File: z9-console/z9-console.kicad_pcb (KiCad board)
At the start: 2 copper layers, 89.5 x 55.5 mm, 130 parts, among them J10 Conn_01x04_Pin, J2 LCD 3.2" 240x320 Conn_01x14_P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, J3 JST GH, J5 ST_STDC14 - SAMTEC_FTSH-107-0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, J6 Screw_Terminal_01x06, J7 TC2070 - TAG Connect, J801 USB_C_Receptacle_USB2.0_16P, Q1 AO3400A, Q2 AO3400A, Q701 AO3400A, SW2 SW_Push, SW3 SW_Push, U1 B0505XT-1WR3, U2 ISO1042-Q1, U22 TLV76733DRVx, U3 STM32F427V_G-I_Tx, U4 ST_SENSOR_2, U5 IIS3DHHCTR, U6 LMR14006YDDCR, U7 SN74LVC1G14DRLR, X2 8MHz 20pF

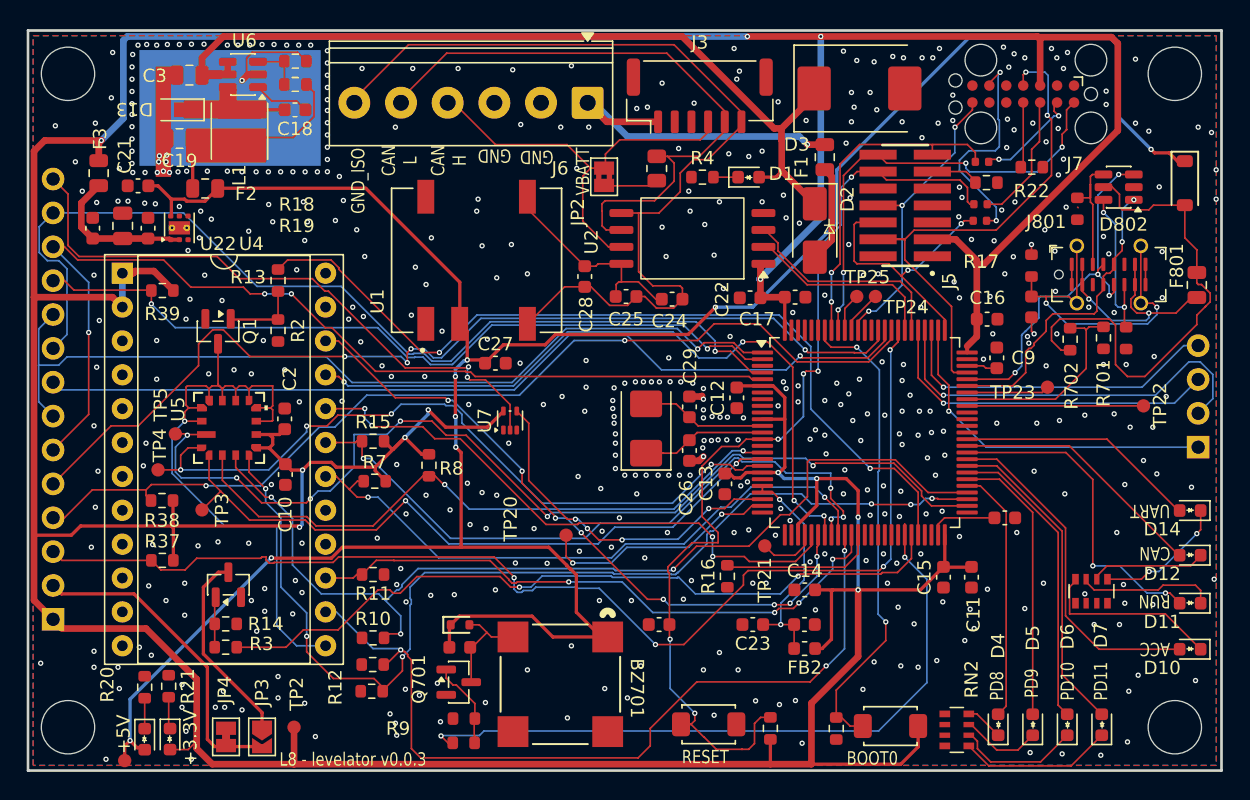
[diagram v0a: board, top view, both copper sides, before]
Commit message: change MEMS device
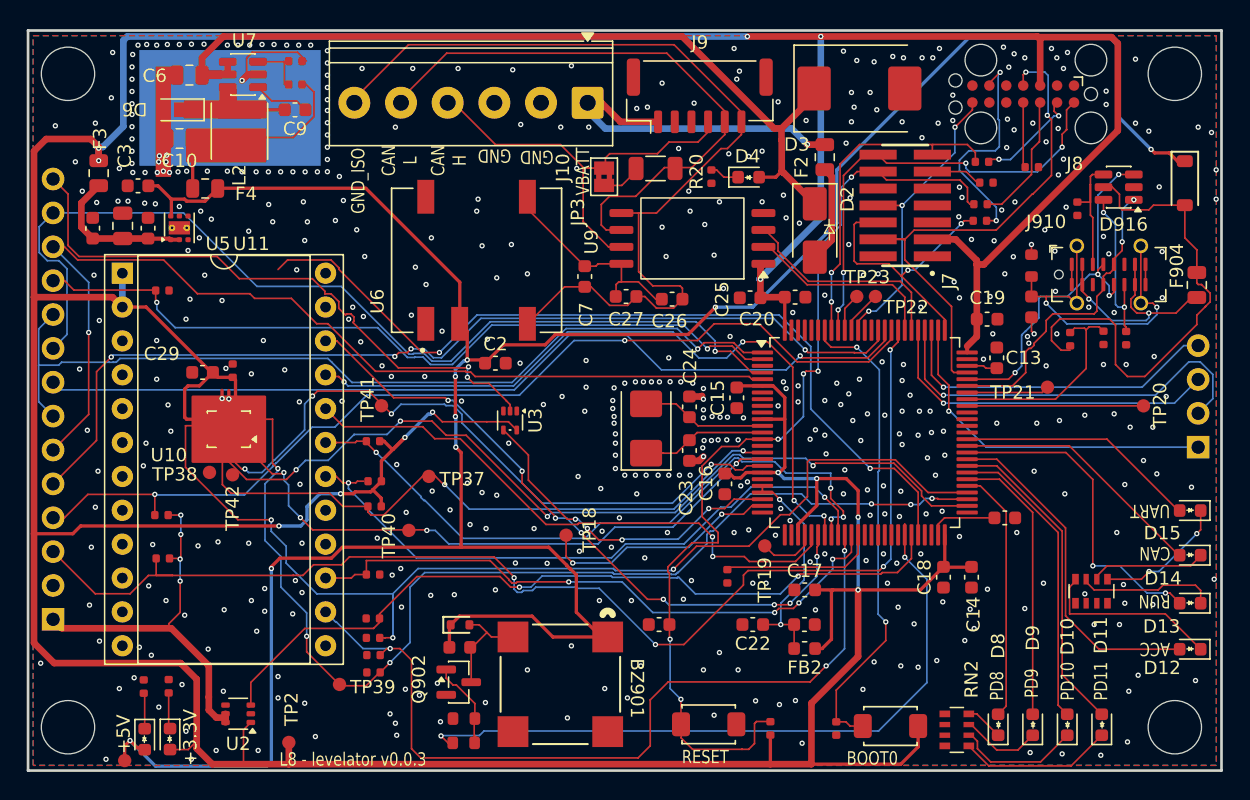
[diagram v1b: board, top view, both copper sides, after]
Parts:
- removed the JP3 at (104.3, 124.8)
- removed JP4: SolderJumper_2_Bridged, Jumper:SolderJumper-2_P1.3mm_Bridged_Pad1.0x1.5mm
- removed Q1, Q2: AO3400A, Package_TO_SOT_SMD:SOT-23
- removed the R13 at (105.5, 90.6)
- removed the R2 at (105.5, 94.3)
- removed the R3 at (101.6, 118.1)
- removed the U5 at (101.8, 101.6)
- added TP37: IIS3DHHCTR_SDI, dnt:TestPoint_Pad_D1.0mm FP .6R, F.Cu at (116.8, 105.2)
- added TP38: IIS3DHHCTR_SDI, dnt:TestPoint_Pad_D1.0mm FP .6R, F.Cu at (100.3, 105.0)
- added TP39: IIS3DHHCTR_SDI, dnt:TestPoint_Pad_D1.0mm FP .6R, F.Cu at (110.1, 120.8)
- added U10: ISM330DHCX, Package_LGA:LGA-14_3x2.5mm_P0.5mm_LayoutBorder3x4y, F.Cu at (101.8, 101.7)
- added U2: TPS22917DBV, dnt:SOT-363_SC-70-6, F.Cu at (102.5, 123.0)
- C28: renamed from C2; footprint Capacitor_SMD:C_0603_1608Metric -> PCM_JLCPCB:C_0402
- R10: renamed from R18; footprint Resistor_SMD:R_0603_1608Metric -> PCM_JLCPCB:R_0402
- R11: renamed from R20; footprint Resistor_SMD:R_0603_1608Metric -> PCM_JLCPCB:R_0402
- R12: renamed from R5; footprint Resistor_SMD:R_0603_1608Metric -> PCM_JLCPCB:R_0402
- R13: renamed from R6; footprint Resistor_SMD:R_0603_1608Metric -> PCM_JLCPCB:R_0402
- R14: renamed from R16; footprint Resistor_SMD:R_0603_1608Metric -> PCM_JLCPCB:R_0402
- R15: renamed from R17; footprint Resistor_SMD:R_0603_1608Metric -> PCM_JLCPCB:R_0402
- R16: renamed from R22; footprint Resistor_SMD:R_0603_1608Metric -> PCM_JLCPCB:R_0402
- R2: renamed from R14; footprint Resistor_SMD:R_0603_1608Metric -> PCM_JLCPCB:R_0402
- R20: renamed from R1; footprint Resistor_SMD:R_0805_2012Metric -> dnt:R_1206_3216Metric
- R21: renamed from R8; footprint Resistor_SMD:R_0603_1608Metric -> PCM_JLCPCB:R_0402
- R22: renamed from R9; footprint Resistor_SMD:R_0603_1608Metric -> PCM_JLCPCB:R_0402
- R23: renamed from R10; footprint Resistor_SMD:R_0603_1608Metric -> PCM_JLCPCB:R_0402
- R24: renamed from R11; footprint Resistor_SMD:R_0603_1608Metric -> PCM_JLCPCB:R_0402
- R25: renamed from R12; footprint Resistor_SMD:R_0603_1608Metric -> PCM_JLCPCB:R_0402
- R26: renamed from R15; footprint Resistor_SMD:R_0603_1608Metric -> PCM_JLCPCB:R_0402
- R27: renamed from R7; footprint Resistor_SMD:R_0603_1608Metric -> PCM_JLCPCB:R_0402
- R3: renamed from R37; footprint Resistor_SMD:R_0603_1608Metric -> PCM_JLCPCB:R_0402
- R4: renamed from R38; footprint Resistor_SMD:R_0603_1608Metric -> PCM_JLCPCB:R_0402
- R5: renamed from R39; footprint Resistor_SMD:R_0603_1608Metric -> PCM_JLCPCB:R_0402
- R7: renamed from R4; footprint Resistor_SMD:R_0603_1608Metric -> PCM_JLCPCB:R_0402
- R8: renamed from R21; footprint Resistor_SMD:R_0603_1608Metric -> PCM_JLCPCB:R_0402
- R9: renamed from R19; footprint Resistor_SMD:R_0603_1608Metric -> PCM_JLCPCB:R_0402
- R930: renamed from R802; footprint PCM_JLCPCB:R_0603 -> PCM_JLCPCB:R_0402
- R931: renamed from R803; value 5.1K -> 5.1kΩ; footprint PCM_JLCPCB:R_0603 -> PCM_JLCPCB:R_0402
- R932: renamed from R702; footprint Resistor_SMD:R_0603_1608Metric -> PCM_JLCPCB:R_0402
- R933: renamed from R701; value 2.2K -> 2.2kΩ; footprint Resistor_SMD:R_0603_1608Metric -> PCM_JLCPCB:R_0402
- moved TP41 17.4 mm to (113.2, 100.0)
- moved TP40 15.6 mm to (115.3, 109.3)
- moved R2 11.0 mm to (112.6, 115.9), turned to 0 degrees
- moved C29 9.86 mm to (99.8, 97.5), turned to 180 degrees
- moved C28 5.32 mm to (102.1, 97.3)
- moved TP42 5.28 mm to (102.1, 105.1)
- moved R21 5.11 mm to (112.7, 107.5), turned to 0 degrees
- moved R22 1.42 mm to (112.7, 120.0)
- moved TP2 1.20 mm to (106.3, 125.2)
- moved R4 1.09 mm to (96.8, 108.2)
- moved R25 0.71 mm to (112.7, 118.7)
- moved R7 0.68 mm to (138.0, 82.8), turned to 90 degrees
- moved R3 0.15 mm to (96.8, 111.4)
- moved R20 0.09 mm to (133.8, 82.2), turned to 180 degrees
- moved R11 0.09 mm to (95.4, 121.0)
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- renumbered BZ701 to BZ901, C19 to C10, C6 to C11, C8 to C12, C9 to C13, C11 to C14, C12 to C15, C13 to C16, C14 to C17, C15 to C18, C16 to C19, C27 to C2, C17 to C20, C20 to C21, C23 to C22, C26 to C23, C29 to C24, C22 to C25, C24 to C26, C25 to C27, C10 to C29, C21 to C3, C5 to C4, C7 to C5, C3 to C6, C28 to C7, C4 to C8, C18 to C9, C701 to C929, C801 to C930, D6 to D10, D7 to D11, D10 to D12, D11 to D13, D12 to D14, D14 to D15, D1 to D4, D9 to D5, D13 to D6, D8 to D7, D4 to D8, D5 to D9, D701 to D915, D802 to D916, D801 to D917, F1 to F2, F2 to F4, F801 to F904, H2 to H901, H3 to H902, H1 to H903, H4 to H904, J6 to J10, J10 to J4, J5 to J7, J7 to J8, J3 to J9, J801 to J910, JP2 to JP3, L1 to L2, Q701 to Q902, R24 to R17, R25 to R18, R26 to R19, R703 to R927, R704 to R928, R801 to R929, TP20 to TP18, TP21 to TP19, TP22 to TP20, TP23 to TP21, TP24 to TP22, TP25 to TP23, TP1 to TP3, TP3 to TP40, TP4 to TP41, TP5 to TP42, U4 to U11, U7 to U3, U22 to U5, U1 to U6, U6 to U7, U3 to U8, U2 to U9
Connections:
- C14 pad 2: +3.3VP -> +3.3V
- C15 pad 2: +3.3VP -> +3.3V
- C16 pad 2: +3.3VP -> +3.3V
- C17 pad 2: +3.3VP -> +3.3V
- C18 pad 2: +3.3VP -> +3.3V
- C19 pad 2: +3.3VP -> +3.3V
- C20 pad 2: +3.3VP -> +3.3V
- C25 pad 1: +3.3VP -> +3.3V
- C28 pad 1: +3.3VP -> +3.3V
- C29 pad 1: +3.3VP -> +3.3V
- D5 pad 2: +3.3VP -> +3.3V
- F3 pad 2: +3.3VP -> +3.3V
- FB2 pad 1: +3.3VP -> +3.3V
- J2 pad 1: +3.3VP -> Net-(J2-VCC)
- J2 pad 2: Net-(J2-GND) -> GND
- J7 pad 3: +3.3VP -> +3.3V
- J8 pad 3: +3.3VP -> +3.3V
- R13 pad 1: +3.3VP -> +3.3V
- R2 pad 2: Net-(Q2-G) -> /LCD_ON
- R21 pad 2: +3.3VP -> +3.3V
- R26 pad 2: +3.3VP -> +3.3V
- R27 pad 2: +3.3VP -> +3.3V
- R3 pad 2: +3.3VP -> Net-(J2-VCC)
- R4 pad 2: +3.3VP -> Net-(J2-VCC)
- R5 pad 2: +3.3VP -> Net-(J2-VCC)
- SW2 pad 2: +3.3VP -> +3.3V
- TP2 pad 1: +3.3VP -> +3.3V
- U11 pad 1: +3.3VP -> +3.3V
- U11 pad 13: Net-(Q1-D) -> GND
- U11 pad 2: +3.3VP -> +3.3V
- U3 pad 5: +3.3VP -> +3.3V
- U8 pad 100: +3.3VP -> +3.3V
- U8 pad 11: +3.3VP -> +3.3V
- U8 pad 19: +3.3VP -> +3.3V
- U8 pad 28: +3.3VP -> +3.3V
- U8 pad 46: /SENSOR_ON -> GND
- U8 pad 50: +3.3VP -> +3.3V
- U8 pad 6: +3.3VP -> +3.3V
- U8 pad 75: +3.3VP -> +3.3V
- U9 pad 1: +3.3VP -> +3.3V
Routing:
- net +3.3V: track 0.00 -> 422.8 mm, vias 0 -> 13
- net +3.3VP: track 417.4 -> 0.00 mm, vias 12 -> 0
- net GND: track 17.6 -> 84.8 mm, vias 492 -> 497
- net /SENSOR_ON: track 63.9 -> 0.00 mm, vias 2 -> 0
- net Net-(Q1-D): track 50.1 -> 0.00 mm, vias 1 -> 0
- net Net-(J2-VCC): track 0.00 -> 30.0 mm, vias 0 -> 4
- net Net-(J2-GND): track 23.7 -> 0.00 mm
- net Net-(JP3-A) (its old number): track 14.7 -> 0.00 mm
- net /SPI2_SCK: track 76.7 -> 66.1 mm, vias 6 -> 4
- net /SPI2_IRQ2: track 73.4 -> 83.4 mm
- net Net-(Q1-G): track 9.00 -> 0.00 mm
- net +5V: track 187.6 -> 195.9 mm
- net /SPI2_SDI: track 51.7 -> 45.9 mm, vias 2 -> 4
- net /SPI2_SDO: track 54.7 -> 50.5 mm
- net /SPI2_IRQ: track 77.8 -> 81.5 mm
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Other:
- board text added: "Keep MEMS heat isolated"

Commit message: console pcb changes
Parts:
- removed the C25 at (140.9, 91.9)
- removed the C26 at (135.0, 92.0)
- removed C27: 100nF, Capacitor_SMD:C_0603_1608Metric
- removed JP3: SolderJumper_2_Bridged, Jumper:SolderJumper-2_P1.3mm_Bridged2Bar_Pad1.0x1.5mm
- removed U9: ISO1042-Q1, Package_SO:SOIC-8_7.5x5.85mm_P1.27mm
- added C12: 100nF, Capacitor_SMD:C_0603_1608Metric, F.Cu at (149.7, 101.0)
- added C13: 100nF, Capacitor_SMD:C_0603_1608Metric, F.Cu at (149.5, 99.6)
- added C951: 100nF, PCM_JLCPCB:C_0603, F.Cu at (140.9, 91.9)
- added C952: 10uF, PCM_JLCPCB:C_0603, F.Cu at (131.6, 91.9)
- added C953: 100nF, PCM_JLCPCB:C_0603, F.Cu at (135.1, 92.0)
- added JP951: SolderJumper_2_Bridged, Jumper:SolderJumper-2_P1.3mm_Bridged2Bar_RoundedPad1.0x1.5mm, F.Cu at (130.1, 82.7)
- added R951: 120R, Resistor_SMD:R_0805_2012Metric, F.Cu at (134.2, 82.2)
- added U951: ISO1042-Q1, Package_SO:SOIC-8_7.5x5.85mm_P1.27mm, F.Cu at (136.5, 87.4)
- R20: value 120R -> 10K; footprint dnt:R_1206_3216Metric -> PCM_JLCPCB:R_0402
- U2: value TPS22917DBV -> TPS22919DCKR
- moved R20 21.2 mm to (124.9, 101.4), turned to 90 degrees
- renumbered BZ901 to BZ701, C19 to C14, C18 to C15, C12 to C16, C13 to C17, C17 to C18, C16 to C19, C15 to C20, C20 to C21, C14 to C22, C21 to C23, C22 to C24, C23 to C25, C24 to C26, C929 to C701, C930 to C801, D915 to D701, D916 to D801, D917 to D802, F904 to F801, J7 to J6, J8 to J7, J910 to J801, Q902 to Q701, R927 to R701, R928 to R702, R929 to R801, R930 to R802, R931 to R803, R932 to R804, R933 to R805
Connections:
- net /can/CAN_H renamed /CAN_H
- J10 pad 5: /can/CAN_L -> /CAN_L
- J9 pad 5: /can/CAN_L -> /CAN_L
- R20 pad 1: /can/CAN_L -> GND
- R20 pad 2: Net-(JP3-A) -> Net-(J2-T_IRQ)
- U8 pad 46: GND -> /MCU/PE15
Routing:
- net GND: track 84.8 -> 20.9 mm, vias 497 -> 495
- net /MCU/PE15: track 0.00 -> 63.9 mm, vias 0 -> 2
- net /can/CAN_L: track 43.2 -> 0.00 mm
- net /CAN_L: track 0.00 -> 43.2 mm
- net Net-(JP3-A): track 4.00 -> 0.00 mm
- net Net-(JP951-A): track 0.00 -> 3.20 mm
- net Net-(J2-T_IRQ): track 45.5 -> 47.4 mm

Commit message: console pcb drc - ready for ism fixups
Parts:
- moved C12 13.0 mm to (141.0, 110.7)
- moved C13 10.5 mm to (139.0, 100.0)
- moved TP19 2.00 mm to (140.5, 109.2)
- moved C20 1.48 mm to (139.0, 98.2), turned to 0 degrees
- moved R951 0.78 mm to (133.7, 81.6)
- moved TP42 0.51 mm to (102.4, 105.5)
- moved TP38 0.26 mm to (100.3, 105.2)
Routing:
- net /MCU/PE15: track 63.9 -> 0.00 mm, vias 2 -> 0
- net Net-(J2-VCC): track 30.0 -> 57.5 mm, vias 4 -> 5
- net +3.3V: track 422.8 -> 428.7 mm
- net /MCU/PA4: track 4.39 -> 7.42 mm
- net /LCD_LED: track 67.2 -> 68.7 mm
- net /VBATT: track 25.6 -> 24.6 mm
- net GND: track 20.9 -> 21.7 mm
- net /SPI4_SDO: track 74.8 -> 75.5 mm
- net /CAN_H: track 31.5 -> 30.8 mm
- net /GND_ISO: track 69.1 -> 68.4 mm
- net /SPI2_SDI: track 45.9 -> 46.5 mm
- net /MCU/NRST: track 72.2 -> 71.6 mm
- net /SPI2_IRQ2: track 83.4 -> 84.0 mm
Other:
- board text removed: "Keep MEMS heat isolated"

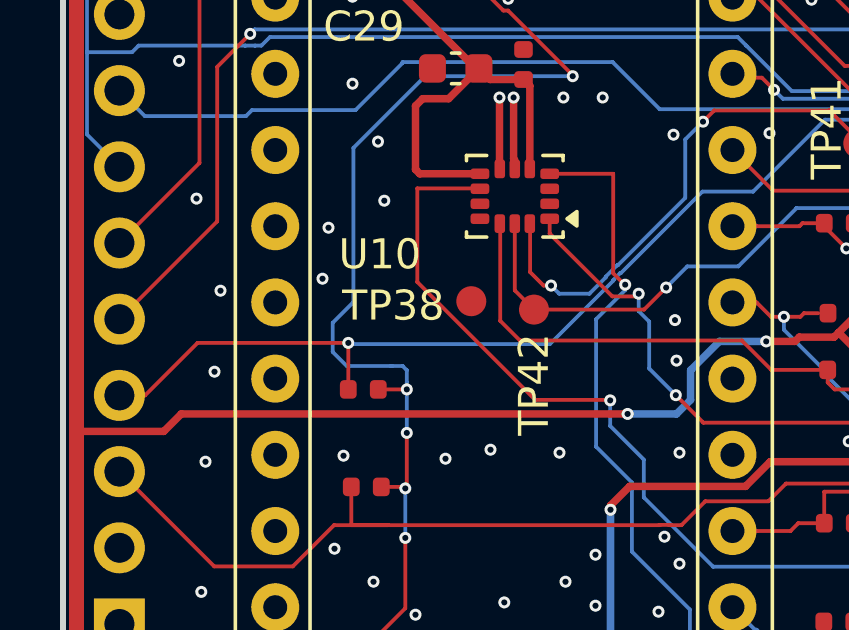
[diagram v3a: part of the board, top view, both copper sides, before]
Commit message: final lcsc mappings
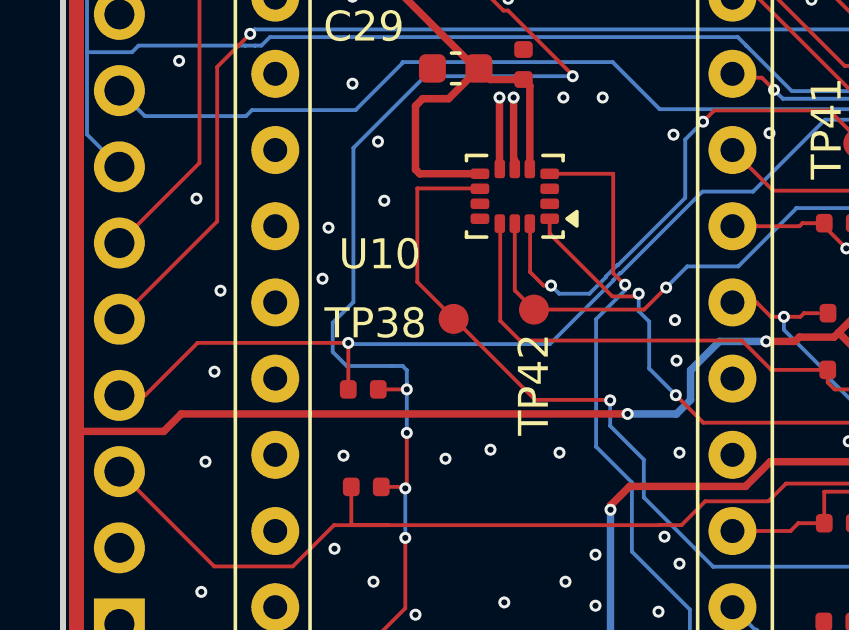
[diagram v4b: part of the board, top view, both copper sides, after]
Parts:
- moved TP38 0.83 mm to (99.8, 105.8)
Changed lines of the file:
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@@
 	(footprint "dnt:TestPoint_Pad_D1.0mm FP .6R"
 		(layer "F.Cu")
-		(at 100.35 105.21)
+		(at 99.76 105.8)
 		(descr "SMD pad as test Point, diameter 1.0mm")
 		(tags "test point SMD pad")

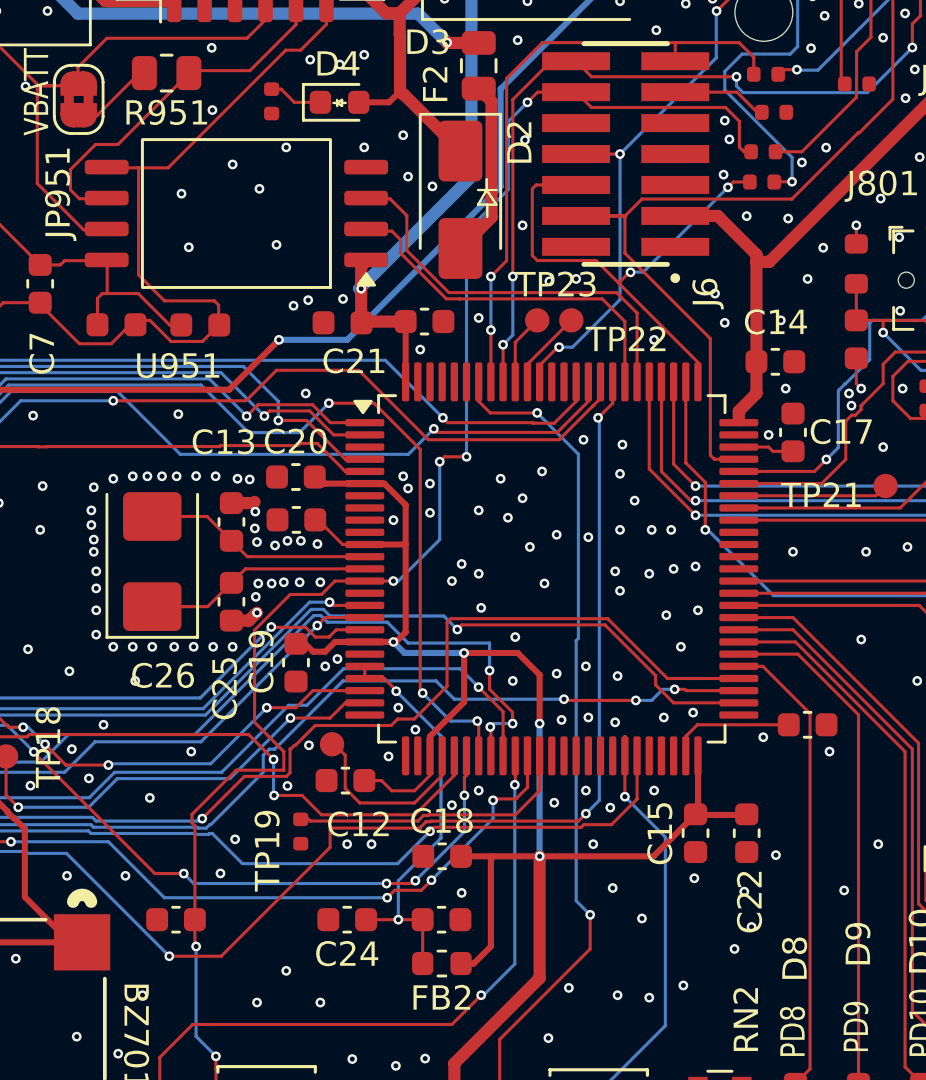
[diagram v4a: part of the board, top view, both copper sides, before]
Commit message: 3d fixes and field removal
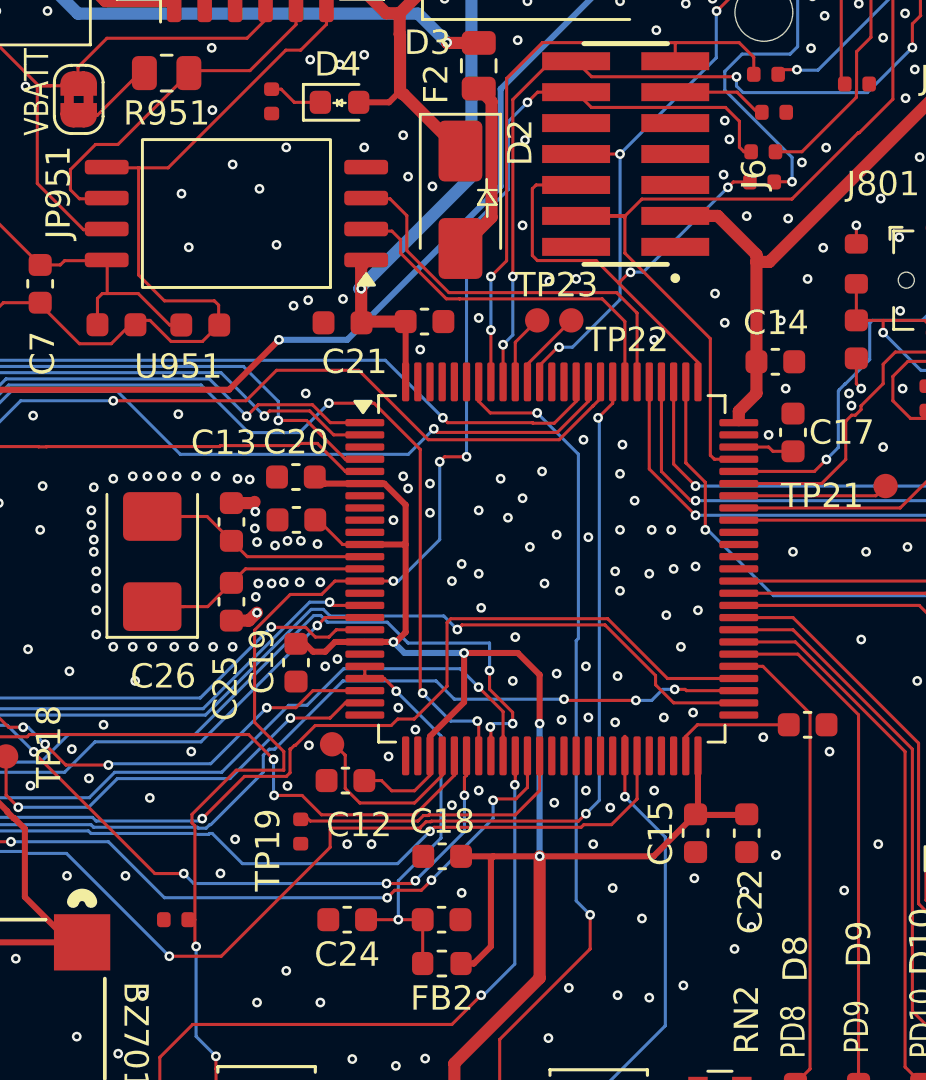
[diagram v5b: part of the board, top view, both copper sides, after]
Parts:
- C11: footprint Capacitor_SMD:C_0603_1608Metric -> PCM_JLCPCB:C_0402
- J6: footprint dnt:SAMTEC_FTSH-107-01-F-DV-K-Fix -> dnt:Conn_SAMTEC_FTSH-107-01-F-DV-K-Fix
